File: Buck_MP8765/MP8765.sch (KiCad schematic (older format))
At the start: 28 parts, among them J1 Jumper

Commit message: ...
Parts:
- DA1: footprint QFN,_DFN,_LGA:FCQFN16 -> QFN,_DFN,_LGA:HFCQFN16
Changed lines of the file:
@@
 EESchema Schematic File Version 4
-EELAYER 26 0
+EELAYER 30 0
 EELAYER END
 $Descr A4 11693 8268
@@
 F 0 "DA1" H 4950 2600 60  0000 C CNN
 F 1 "MP8765" H 4950 2500 60  0000 C CNN
-F 2 "QFN,_DFN,_LGA:FCQFN16" H 5250 1400 60  0001 C CNN
+F 2 "QFN,_DFN,_LGA:HFCQFN16" H 5250 1400 60  0001 C CNN
 F 3 "" H 5200 1600 60  0000 C CNN
 F 4 "16" H 4650 2600 60  0001 C CNN "SolderPoints"

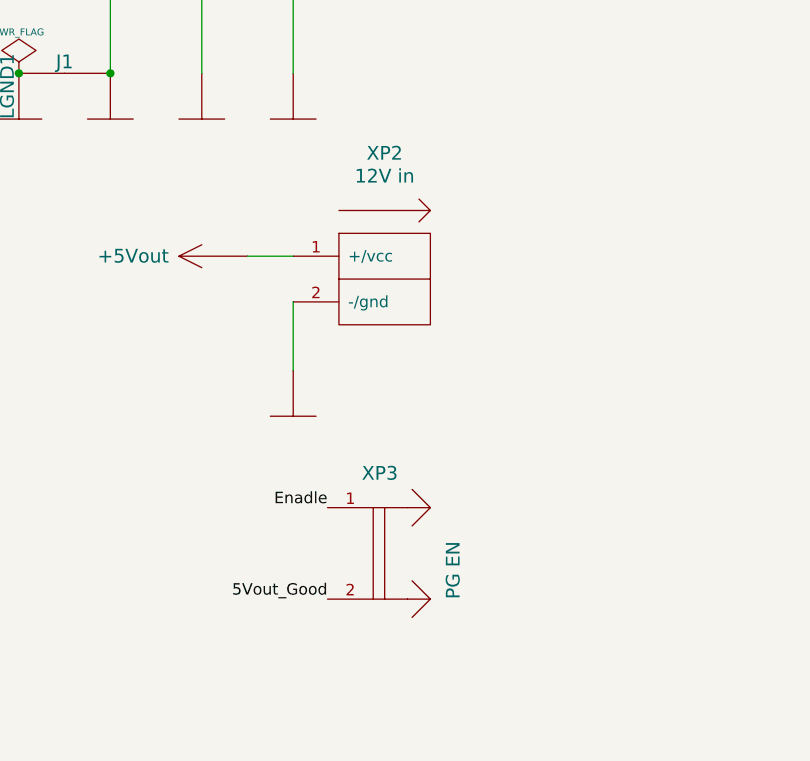
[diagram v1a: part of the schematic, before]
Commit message: модуль MP8765 завершён
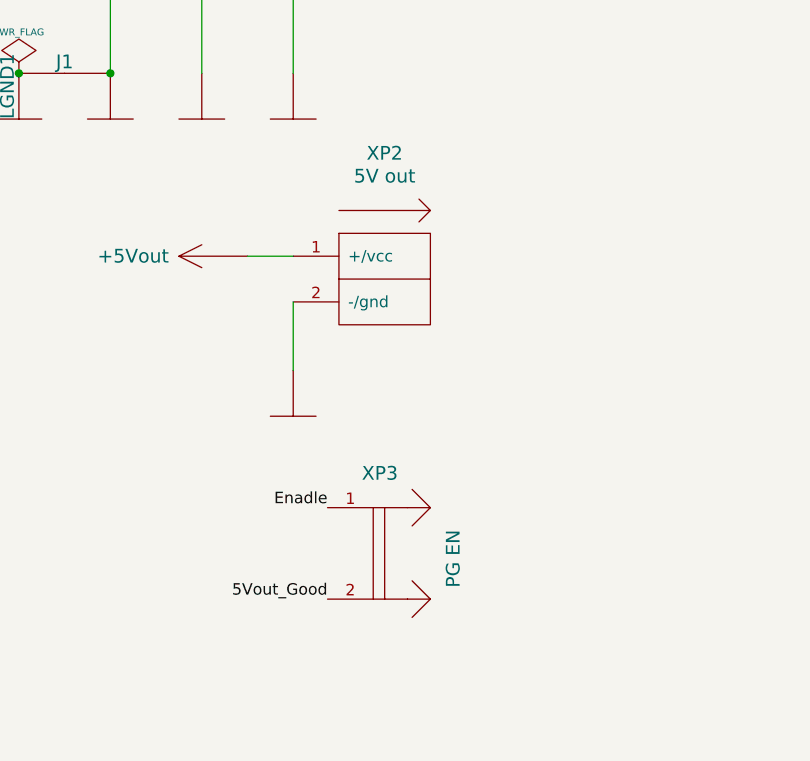
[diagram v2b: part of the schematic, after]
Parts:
- XP2: value 12V in -> 5V out
- XP3: value PG EN -> PG EN
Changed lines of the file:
@@
 P 10150 4300
 F 0 "XP2" H 10150 4850 60  0000 C CNN
-F 1 "12V in" H 10150 4750 60  0000 C CNN
+F 1 "5V out" H 10150 4750 60  0000 C CNN
 F 2 "Connectors:for_PolarOut_MicroFit-1x2" H 10150 4050 60  0001 C CNN
 F 3 "" H 10200 3950 60  0000 C CNN
@@
 P 10250 5500
 F 0 "XP3" H 10050 5850 60  0000 L CNN
-F 1 "PG   EN" V 10450 5300 60  0000 L CNN
+F 1 "PG  EN" V 10450 5350 60  0000 L CNN
 F 2 "Connectors:PLS-2" H 10100 5250 60  0001 C CNN
 F 3 "" H 10350 5700 60  0000 C CNN

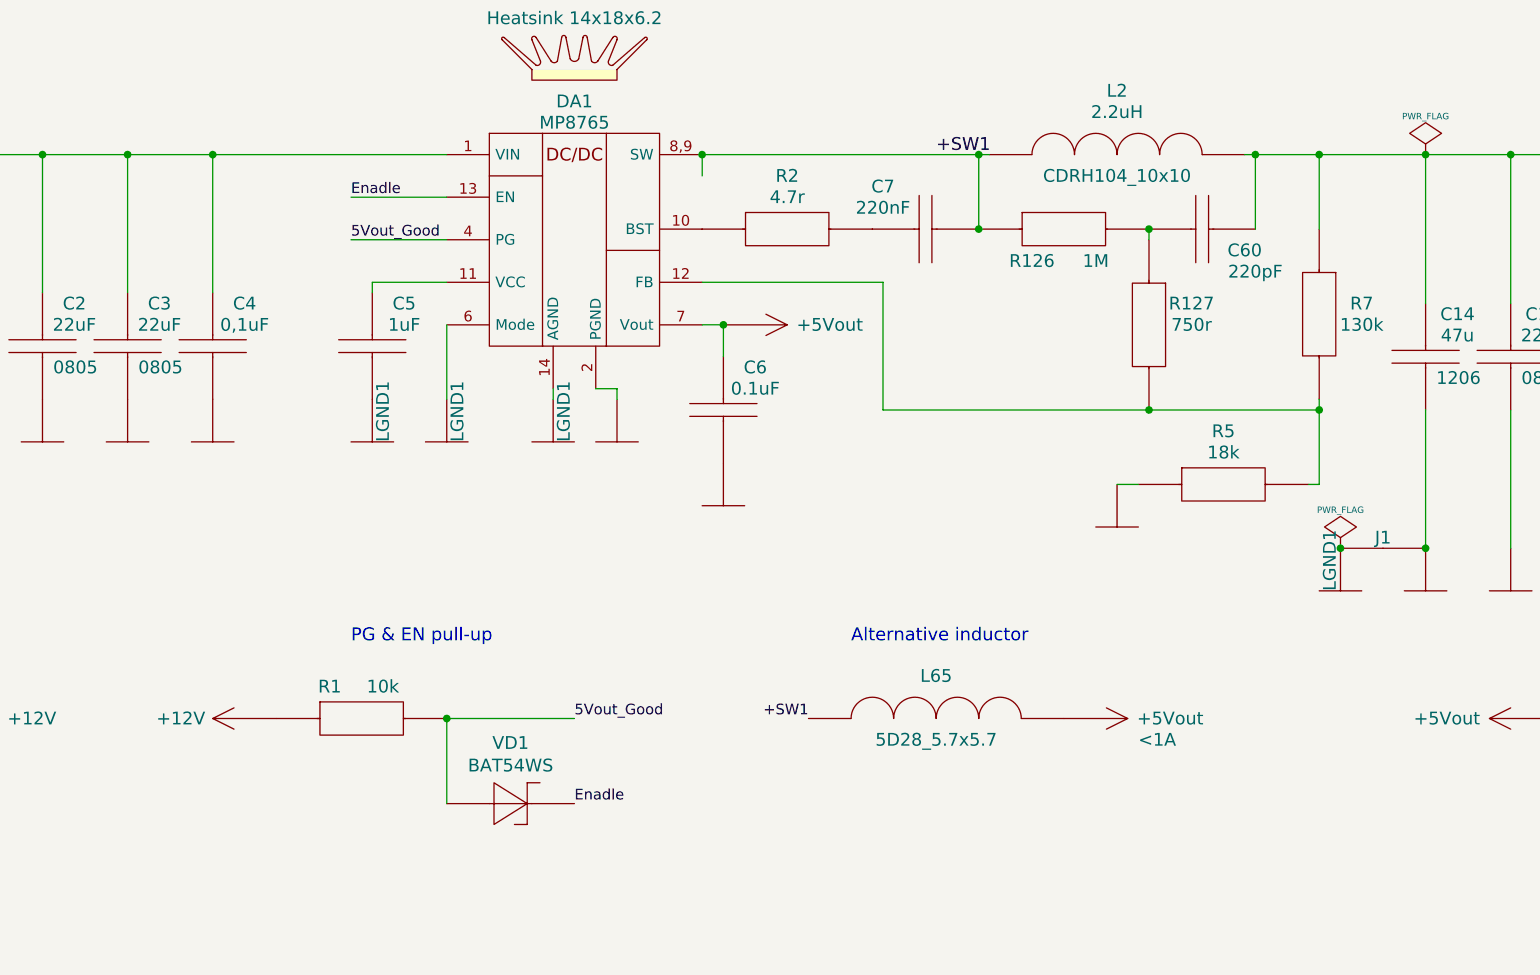
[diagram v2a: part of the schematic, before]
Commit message: + результаты тестов и правки
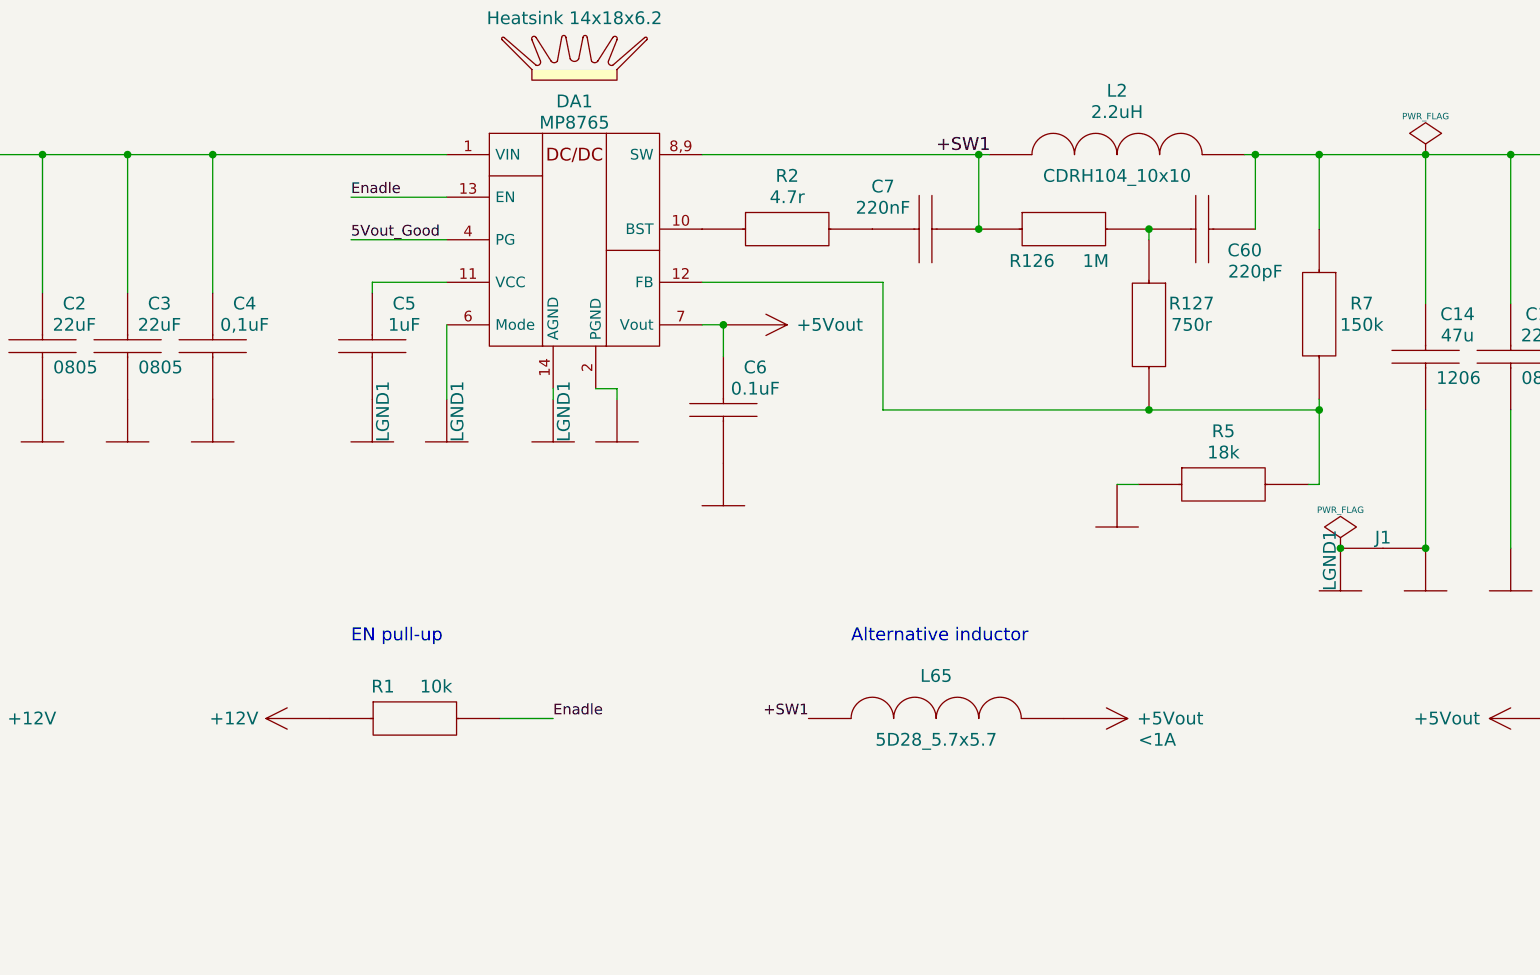
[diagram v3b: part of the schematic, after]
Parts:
- removed VD1: BAT54WS, Diodes:SOD323, symbol Diodes:BAT54WS
- R7: value 130k -> 150k
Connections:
- net 5Vout_Good: no longer R1.2
- net Enadle: now also R1.2
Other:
- note added: "EN pull-up"
- note removed: "PG & EN pull-up"
- moved on the sheet: R1
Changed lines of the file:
@@
 L Resistors:R_0603 R1
 U 1 2 5F9683BF
-P 4100 3950
-F 0 "R1" V 4000 4250 60  0000 C CNN
-F 1 "10k" V 4000 4000 60  0000 C CNN
-F 2 "Resistors:RES0603" H 4100 3800 60  0001 C CNN
-F 3 "" H 3700 3950 60  0000 C CNN
-	1    4100 3950
+P 4350 3950
+F 0 "R1" V 4250 4250 60  0000 C CNN
+F 1 "10k" V 4250 4000 60  0000 C CNN
+F 2 "Resistors:RES0603" H 4350 3800 60  0001 C CNN
+F 3 "" H 3950 3950 60  0000 C CNN
+	1    4350 3950
 	0    -1   -1   0
 $EndComp
@@
 P 8450 2300
 F 0 "R7" V 8400 2500 60  0000 C CNN
-F 1 "130k" V 8500 2500 60  0000 C CNN
+F 1 "150k" V 8500 2500 60  0000 C CNN
 F 2 "Resistors:RES0603" H 8450 2150 60  0001 C CNN
 F 3 "" H 8050 2300 60  0000 C CNN
@@
 	1    0    0    -1
 $EndComp
-Wire Wire Line
-	5550 1650 5550 1550
-Connection ~ 5550 1550
 Connection ~ 6850 1900
 Wire Wire Line
@@
 Text Label 3900 1750 0    50   ~ 0
 Enadle
-Text Label 4950 4600 0    50   ~ 0
+Text Label 4850 4200 0    50   ~ 0
 Enadle
-Text Label 4950 4200 0    50   ~ 0
-5Vout_Good
 $Comp
 L Power:+12V #U0102
 U 1 1 5F347B2C
-P 3550 4200
-F 0 "#U0102" H 3600 4250 60  0001 C CNN
-F 1 "+12V" H 4000 4200 60  0000 C CNN
-F 2 "" H 3550 4200 60  0000 C CNN
-F 3 "" H 3550 4200 60  0000 C CNN
-	1    3550 4200
+P 3800 4200
+F 0 "#U0102" H 3850 4250 60  0001 C CNN
+F 1 "+12V" H 4250 4200 60  0000 C CNN
+F 2 "" H 3800 4200 60  0000 C CNN
+F 3 "" H 3800 4200 60  0000 C CNN
+	1    3800 4200
 	-1   0    0    1
 $EndComp
-$Comp
-L Diodes:BAT54WS VD1
-U 1 1 5F3489BD
-P 4650 4600
-F 0 "VD1" H 4650 4885 60  0000 C CNN
-F 1 "BAT54WS" H 4650 4779 60  0000 C CNN
-F 2 "Diodes:SOD323" H 4650 4450 60  0001 C CNN
-F 3 "" H 4350 4600 60  0000 C CNN
-F 4 "2" H 4400 4900 60  0001 C CNN "SolderPoints"
-F 5 "0" H 4400 4800 60  0001 C CNN "SolderPoints_DIP"
-	1    4650 4600
-	1    0    0    -1
-$EndComp
-Wire Wire Line
-	4950 4200 4350 4200
-Wire Wire Line
-	4350 4600 4350 4200
-Connection ~ 4350 4200
+Wire Wire Line
+	4850 4200 4600 4200
 Text Notes 3900 3850 0    61   ~ 0
-PG & EN pull-up
+EN pull-up
 $Comp
 L Connectors:for_PolarOut XP1

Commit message: Переоткрыты схемы
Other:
- note added: "MP8765 Module"
- note removed: "Квест-контроллер"
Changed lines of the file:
@@
 $EndComp
 Text Notes 7050 6850 0    197  ~ 0
-Квест-контроллер
+MP8765 Module
 Wire Wire Line
 	2450 2200 2450 1550
